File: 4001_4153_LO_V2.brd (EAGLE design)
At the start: 109 x 63 mm, 112 parts, among them IC1 74LVC2G17GV,125, IC10 MCP6H01, IC2 74LVC2G17GV,125, IC3 74LVC2G17GV,125, IC4 ADF4001BRUZ, IC5 ATTINY45V-10SU, IC6 7805DT, IC7 7809DT, IC8 LD117ASTR, IC9 ADF4153BRUZ-RL7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

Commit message: Tracking
Rotated 5v reg
tracking around output device
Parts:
- moved C41 0.38 mm to (94.5, 34.5)
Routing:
- net GND: track 64.2 -> 65.1 mm
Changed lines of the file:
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@@
 <layers>
 <layer number="1" name="Top" color="4" fill="1" visible="yes" active="yes"/>
-<layer number="2" name="RFEarth" color="1" fill="3" visible="no" active="yes"/>
+<layer number="2" name="RFEarth" color="1" fill="3" visible="yes" active="yes"/>
 <layer number="3" name="Route3" color="4" fill="3" visible="no" active="no"/>
 <layer number="4" name="Route4" color="1" fill="4" visible="no" active="no"/>
@@
 <layer number="13" name="Route13" color="4" fill="5" visible="no" active="no"/>
 <layer number="14" name="Route14" color="1" fill="6" visible="no" active="no"/>
-<layer number="15" name="Signal" color="4" fill="3" visible="no" active="yes"/>
+<layer number="15" name="Signal" color="4" fill="3" visible="yes" active="yes"/>
 <layer number="16" name="Power" color="1" fill="1" visible="yes" active="yes"/>
 <layer number="17" name="Pads" color="2" fill="1" visible="yes" active="yes"/>
@@
 <layer number="28" name="bValues" color="7" fill="1" visible="no" active="yes"/>
 <layer number="29" name="tStop" color="7" fill="3" visible="no" active="yes"/>
-<layer number="30" name="bStop" color="7" fill="6" visible="no" active="yes"/>
+<layer number="30" name="bStop" color="7" fill="6" visible="yes" active="yes"/>
 <layer number="31" name="tCream" color="7" fill="4" visible="no" active="yes"/>
 <layer number="32" name="bCream" color="7" fill="5" visible="no" active="yes"/>
@@
 <rectangle x1="88.854" y1="32.084" x2="123.854" y2="37.084" layer="30" rot="R90"/>
 <text x="4.863" y="3.556" size="1.016" layer="21" rot="R90">EXT REF</text>
-<text x="4.767" y="10.302" size="1.016" layer="21" rot="R90">EXT LOCK</text>
-<text x="4.798" y="18.2004" size="1.016" layer="21" rot="R90">VCO LOCK</text>
+<text x="4.767" y="18.302" size="1.016" layer="21" rot="R90">EXT LOCK</text>
+<text x="4.798" y="10.2004" size="1.016" layer="21" rot="R90">VCO LOCK</text>
 <wire x1="0" y1="53" x2="0" y2="1" width="0" layer="20"/>
 <wire x1="0" y1="1" x2="0" y2="-10" width="0" layer="20"/>
@@
 <rectangle x1="86" y1="50" x2="87" y2="53" layer="30"/>
 <rectangle x1="87" y1="49" x2="104" y2="53" layer="30"/>
+<rectangle x1="27" y1="0" x2="35" y2="9" layer="30"/>
 </plain>
 <attributes>
@@
 <attribute name="VALUE" x="98.0299" y="35.5929" size="1.27" layer="27" rot="R90"/>
 </element>
-<element name="C41" library="resistor" package="C0603" value="100pF" x="94.1672" y="34.492921875" smashed="yes">
-<attribute name="NAME" x="94.2942" y="32.460921875" size="1.27" layer="25"/>
-<attribute name="VALUE" x="93.2782" y="32.460921875" size="1.27" layer="27"/>
+<element name="C41" library="resistor" package="C0603" value="100pF" x="94.5482" y="34.492921875" smashed="yes">
+<attribute name="NAME" x="94.6752" y="32.460921875" size="1.27" layer="25"/>
+<attribute name="VALUE" x="93.6592" y="32.460921875" size="1.27" layer="27"/>
 </element>
 <element name="C31" library="resistor" package="C0603" value="1uF" x="91.521103125" y="41.4965625" smashed="yes" rot="R180">
@@
 <wire x1="43.559" y1="29.489" x2="42.480353125" y2="29.489" width="1.016" layer="1"/>
 <wire x1="42.480353125" y1="29.489" x2="42.288025" y2="29.296671875" width="1.016" layer="1"/>
-<wire x1="90.294071875" y1="34.4852375" x2="89.17449375" y2="34.4852375" width="1.27" layer="1"/>
 <wire x1="89.17449375" y1="34.4852375" x2="89.056546875" y2="34.603184375" width="1.27" layer="1"/>
 <contactref element="C15" pad="2"/>
@@
 <via x="25.803953125" y="8.870415625" extent="1-16" drill="0.8" shape="square"/>
 <via x="36.049753125" y="8.862015625" extent="1-16" drill="0.8" shape="square"/>
+<wire x1="90.294071875" y1="34.4852375" x2="89.2127625" y2="34.4852375" width="0.6096" layer="1"/>
+<wire x1="89.2127625" y1="34.4852375" x2="89.1286" y2="34.5694" width="0.6096" layer="1"/>
+<wire x1="89.1286" y1="34.5694" x2="89.1286" y2="34.8714" width="0.6096" layer="1"/>
+<wire x1="89.1286" y1="34.8714" x2="89" y2="35" width="0.6096" layer="1"/>
+<wire x1="89.17449375" y1="34.4852375" x2="89.17449375" y2="34.82550625" width="0.6096" layer="1"/>
+<wire x1="89.17449375" y1="34.82550625" x2="89.1286" y2="34.8714" width="0.6096" layer="1"/>
 </signal>
 <signal name="+9V">
@@
 <wire x1="93.9776" y1="32.6729375" x2="93.862121875" y2="32.557459375" width="0.6096" layer="1"/>
 <wire x1="91.994071875" y1="34.4852375" x2="93.309515625" y2="34.4852375" width="0.6096" layer="1"/>
-<wire x1="93.309515625" y1="34.4852375" x2="93.3172" y2="34.492921875" width="0.6096" layer="1"/>
+<wire x1="93.309515625" y1="34.4852375" x2="93.6982" y2="34.492921875" width="0.6096" layer="1"/>
 <wire x1="93.9776" y1="32.6729375" x2="93.9776" y2="33.1748" width="0.6096" layer="1"/>
 <wire x1="93.9776" y1="33.1748" x2="93.472" y2="33.6804" width="0.6096" layer="1"/>
 <wire x1="93.472" y1="33.6804" x2="93.472" y2="34.338121875" width="0.6096" layer="1"/>
-<wire x1="93.472" y1="34.338121875" x2="93.3172" y2="34.492921875" width="0.6096" layer="1"/>
+<wire x1="93.472" y1="34.338121875" x2="93.6982" y2="34.492921875" width="0.6096" layer="1"/>
 </signal>
 <signal name="+5V">
@@
 <contactref element="C41" pad="2"/>
 <contactref element="R17" pad="1"/>
-<wire x1="95.0172" y1="34.492921875" x2="97.303721875" y2="34.492921875" width="0.6096" layer="1"/>
+<wire x1="95.3982" y1="34.492921875" x2="97.303721875" y2="34.492921875" width="0.6096" layer="1"/>
 <wire x1="97.303721875" y1="34.492921875" x2="97.368" y2="34.5572" width="0.6096" layer="1"/>
 </signal>

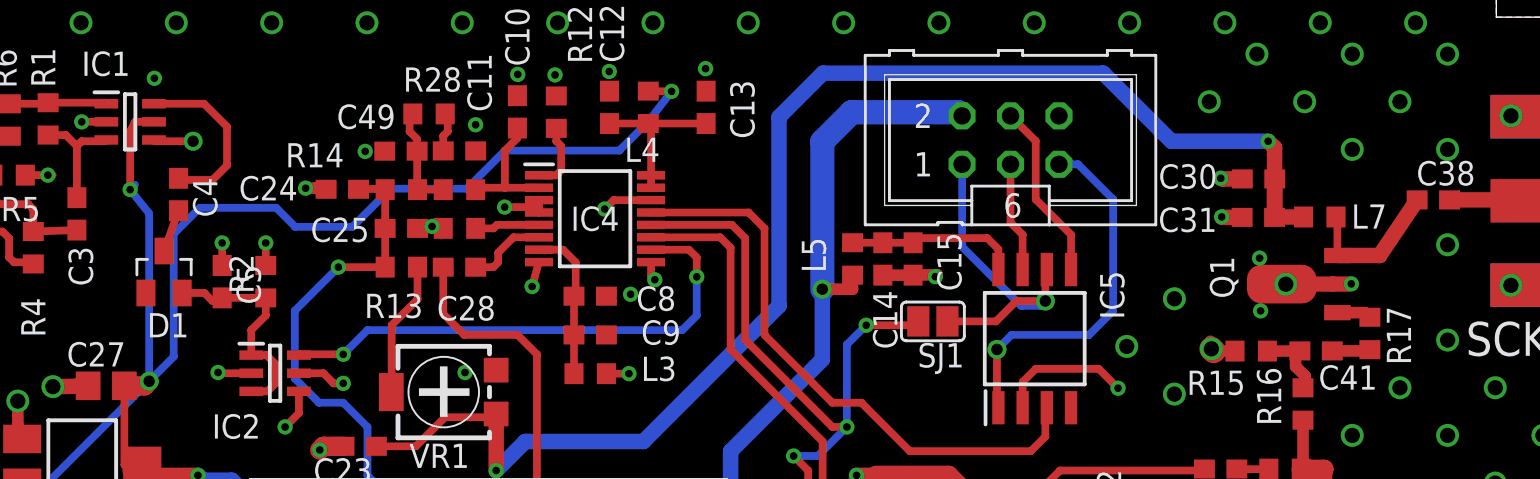
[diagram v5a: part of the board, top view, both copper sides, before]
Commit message: Output and detector
Moved resistor in output stage to power feed
Swapped C for R in 10MHz detector
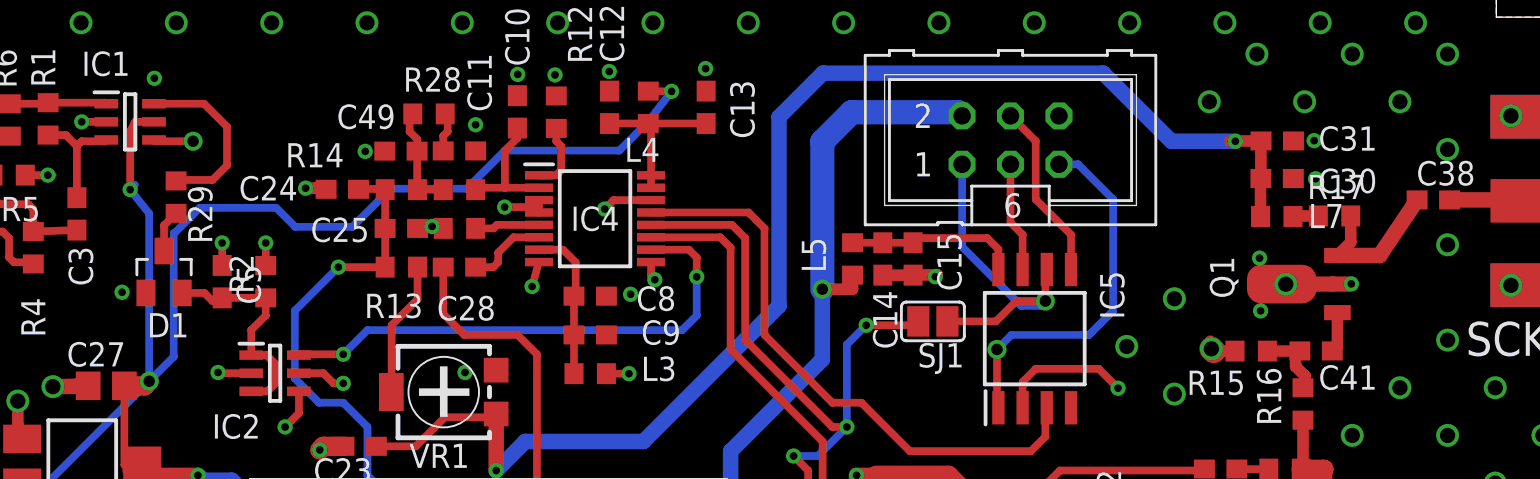
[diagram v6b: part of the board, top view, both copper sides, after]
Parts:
- removed C4: 100nF, resistor:C0603
- added R29: 100K, rcl:R0603
- IC8: value LD117ASTR -> LD1117AS33TR
- moved R17 6.44 mm to (95.5, 41.6), turned to 180 degrees
- moved C31 4.13 mm to (92.5, 45.5), turned to 0 degrees
- moved L7 2.26 mm to (92.5, 41.5)
- moved C30 0.97 mm to (92.5, 43.5), turned to 0 degrees
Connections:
- net N$11: now also C41.2; no longer R17.2
- net N$12: now also R17.1; no longer L7.1
- net N$21: now also L7.1, R17.2; no longer C41.2, R17.1
- net N$23: now also R29.2; no longer C4.2
- net N$30: now also R29.1; no longer C4.1
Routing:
- net +5V: track 136.2 -> 132.7 mm
- net GND: track 65.1 -> 62.9 mm
- net N$21: track 2.00 -> 1.34 mm

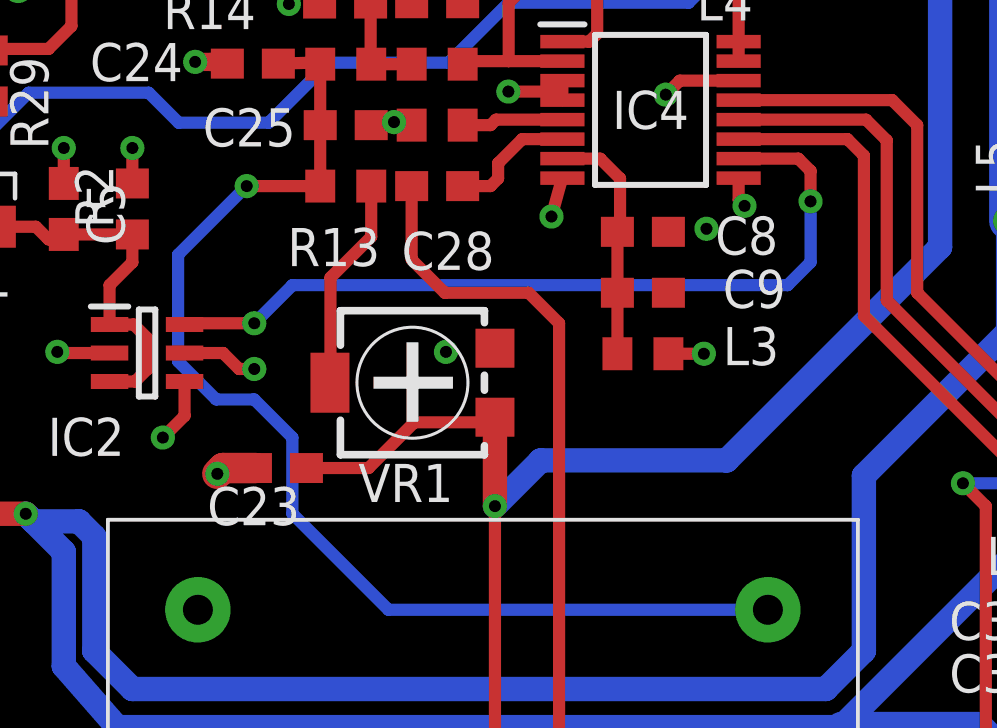
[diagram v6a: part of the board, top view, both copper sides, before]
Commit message: multi-turn
replaced single turn pot with multiturn
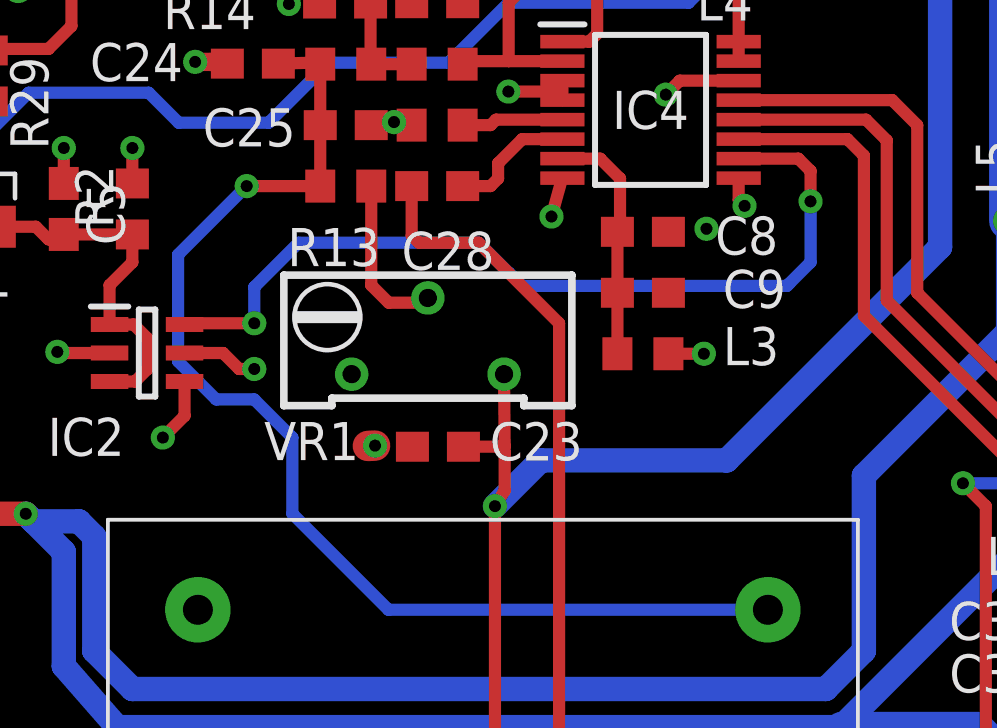
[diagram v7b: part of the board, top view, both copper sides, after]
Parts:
- VR1: value 1K -> (none); device resistor:RTRIM4G/J -> resistor:RTRIM64Y
- moved C23 5.28 mm to (49.6, 30.2)
- moved VR1 0.59 mm to (49.3, 32.6), turned to 270 degrees
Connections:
- net +5V: now also VR1.3; no longer VR1.1
- net GND: now also VR1.1; no longer VR1.3
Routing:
- net +5V: track 132.7 -> 128.7 mm
- net N$19: track 8.60 -> 5.50 mm
- net SDVDD1: track 27.3 -> 29.2 mm
- net GND: track 62.9 -> 61.8 mm, vias 188 -> 187
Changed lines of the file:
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@@
 <layers>
 <layer number="1" name="Top" color="4" fill="1" visible="yes" active="yes"/>
-<layer number="2" name="RFEarth" color="1" fill="3" visible="no" active="yes"/>
+<layer number="2" name="RFEarth" color="1" fill="3" visible="yes" active="yes"/>
 <layer number="3" name="Route3" color="4" fill="3" visible="no" active="no"/>
 <layer number="4" name="Route4" color="1" fill="4" visible="no" active="no"/>
@@
 <layer number="13" name="Route13" color="4" fill="5" visible="no" active="no"/>
 <layer number="14" name="Route14" color="1" fill="6" visible="no" active="no"/>
-<layer number="15" name="Signal" color="4" fill="3" visible="no" active="yes"/>
-<layer number="16" name="Power" color="1" fill="1" visible="yes" active="yes"/>
+<layer number="15" name="Signal" color="4" fill="3" visible="yes" active="yes"/>
+<layer number="16" name="Power" color="1" fill="1" visible="no" active="yes"/>
 <layer number="17" name="Pads" color="2" fill="1" visible="yes" active="yes"/>
 <layer number="18" name="Vias" color="2" fill="1" visible="yes" active="yes"/>
@@
 <attribute name="VALUE" x="18.172696875" y="22.532253125" size="1.27" layer="27"/>
 </element>
-<element name="VR1" library="resistor" package="RTRIM4G/J" value="1K" x="48.791759375" y="32.33279375" smashed="yes" rot="R90">
-<attribute name="NAME" x="46.988921875" y="28.3563375" size="1.27" layer="25"/>
-<attribute name="VALUE" x="51.331759375" y="36.37779375" size="1.27" layer="27" rot="R180"/>
-</element>
 <element name="IC8" library="v-reg" package="SOT223" value="LD1117AS33TR" x="29.83038125" y="27.5757625" smashed="yes" rot="R270">
 <attribute name="NAME" x="32.1142375" y="23.78518125" size="1.27" layer="25"/>
@@
 <attribute name="VALUE" x="79.496853125" y="13.551221875" size="1.27" layer="27" rot="R180"/>
 </element>
-<element name="C23" library="rcl" package="C0603" value="100nF" x="44.409" y="29.489" rot="R180"/>
+<element name="C23" library="rcl" package="C0603" value="100nF" x="49.6414" y="30.2002" smashed="yes" rot="R180">
+<attribute name="NAME" x="51.3744" y="29.7438" size="1.27" layer="25"/>
+<attribute name="VALUE" x="50.2764" y="32.1052" size="1.27" layer="27" rot="R180"/>
+</element>
 <element name="C14" library="resistor" package="C0603" value="1uF" x="71.823" y="39.3165" smashed="yes" rot="R270">
 <attribute name="NAME" x="71.315" y="37.6655" size="1.27" layer="25" rot="R270"/>
@@
 </element>
 <element name="R29" library="rcl" package="R0603" value="100K" x="34.752" y="42.559" rot="R270"/>
+<element name="VR1" library="resistor" package="RTRIM64Y" value="" x="49.3054" y="32.6186" smashed="yes" rot="R270">
+<attribute name="NAME" x="43.8474" y="29.753" size="1.27" layer="25"/>
+<attribute name="VALUE" x="44.3554" y="29.8686" size="1.27" layer="27"/>
+</element>
 </elements>
 <signals>
@@
 <contactref element="C20" pad="2"/>
 <contactref element="IC7" pad="3"/>
-<contactref element="VR1" pad="3"/>
 <via x="14.137003125" y="19.927146875" extent="1-16" drill="0.4" shape="square"/>
 <contactref element="C26" pad="2"/>
@@
 <via x="107.308184375" y="37.931953125" extent="1-16" drill="0.8" shape="square"/>
 <contactref element="C23" pad="2"/>
-<via x="42.288025" y="29.296671875" extent="1-16" drill="0.4" shape="square"/>
-<wire x1="43.559" y1="29.489" x2="42.480353125" y2="29.489" width="1.016" layer="1"/>
-<wire x1="42.480353125" y1="29.489" x2="42.288025" y2="29.296671875" width="1.016" layer="1"/>
+<via x="47.545825" y="30.236471875" extent="1-16" drill="0.4" shape="square"/>
+<wire x1="47.306353125" y1="30.2256" x2="47.545825" y2="30.236471875" width="1.016" layer="1"/>
 <wire x1="89.17449375" y1="34.4852375" x2="89.056546875" y2="34.603184375" width="1.27" layer="1"/>
 <contactref element="C15" pad="2"/>
@@
 <wire x1="38.696" y1="33.323" x2="36.991696875" y2="33.323" width="0.4064" layer="1"/>
 <wire x1="36.991696875" y1="33.323" x2="36.954025" y2="33.360671875" width="0.4064" layer="1"/>
-<via x="49.908025" y="33.360671875" extent="1-16" drill="0.4" shape="square"/>
 <wire x1="53.79" y1="41.752" x2="53.79" y2="42.402" width="0.4064" layer="1"/>
 <wire x1="53.607" y1="41.935" x2="53.79" y2="41.752" width="0.4064" layer="1"/>
@@
 <via x="94.520909375" y="43.5214625" extent="1-16" drill="0.4" shape="square"/>
 <via x="31.92" y="37.5712" extent="1-16" drill="0.4" shape="square"/>
+<contactref element="VR1" pad="1"/>
 </signal>
 <signal name="+9V">
@@
 <contactref element="C30" pad="1"/>
 <contactref element="C31" pad="1"/>
-<contactref element="VR1" pad="1"/>
 <contactref element="C23" pad="1"/>
 <contactref element="OSC1" pad="VCC"/>
@@
 <wire x1="48.6" y1="5.613" x2="41.792" y2="5.613" width="0.4064" layer="1"/>
 <wire x1="41.792" y1="5.613" x2="41.64" y2="5.765" width="0.4064" layer="1"/>
-<wire x1="45.259" y1="29.489" x2="47.33" y2="29.489" width="0.4064" layer="1"/>
-<wire x1="47.33" y1="29.489" x2="48.854" y2="31.013" width="0.4064" layer="1"/>
-<wire x1="48.854" y1="31.013" x2="51.371965625" y2="31.013" width="0.4064" layer="1"/>
-<wire x1="51.371965625" y1="31.013" x2="51.541759375" y2="31.18279375" width="0.4064" layer="1"/>
 <via x="90.3134" y="45.491" extent="1-16" drill="0.4" shape="octagon"/>
 <wire x1="90.3134" y1="45.491" x2="86.954" y2="45.491" width="0.8128" layer="16"/>
@@
 <wire x1="53.065759375" y1="29.743" x2="51.541759375" y2="28.219" width="0.8128" layer="16"/>
 <via x="51.541759375" y="28.219" extent="1-16" drill="0.4" shape="octagon"/>
-<wire x1="51.541759375" y1="28.219" x2="51.541759375" y2="31.18279375" width="0.8128" layer="1"/>
 <contactref element="IC6" pad="2"/>
 <contactref element="C17" pad="1"/>
@@
 <wire x1="91.661296875" y1="45.5050375" x2="90.0480375" y2="45.5050375" width="0.6096" layer="1"/>
 <wire x1="90.0480375" y1="45.5050375" x2="90.3134" y2="45.491" width="0.6096" layer="1"/>
+<contactref element="VR1" pad="3"/>
+<wire x1="51.8654" y1="30.2256" x2="51.8454" y2="32.6186" width="0.4064" layer="1"/>
+<wire x1="51.8654" y1="30.2256" x2="51.8654" y2="30" width="0.4064" layer="1"/>
+<wire x1="51.8654" y1="30" x2="51.8654" y2="28.733559375" width="0.4064" layer="1"/>
+<wire x1="51.8654" y1="28.733559375" x2="51.541759375" y2="28.219" width="0.4064" layer="1"/>
+<wire x1="50.4914" y1="30.2002" x2="51.6652" y2="30.2002" width="0.4064" layer="1"/>
+<wire x1="51.6652" y1="30.2002" x2="51.8654" y2="30" width="0.4064" layer="1"/>
 </signal>
 <signal name="OUTPUT">
@@
 <contactref element="C28" pad="2"/>
 <contactref element="OSC1" pad="OUT"/>
-<wire x1="48.766" y1="38.887" x2="48.766" y2="36.435" width="0.4064" layer="1"/>
-<wire x1="48.766" y1="36.435" x2="49.87" y2="35.331" width="0.4064" layer="1"/>
-<wire x1="49.87" y1="35.331" x2="52.664" y2="35.331" width="0.4064" layer="1"/>
-<wire x1="52.664" y1="35.331" x2="53.68" y2="34.315" width="0.4064" layer="1"/>
 <wire x1="53.68" y1="34.315" x2="53.68" y2="10.693" width="0.4064" layer="1"/>
 <wire x1="53.68" y1="10.693" x2="58.76" y2="5.613" width="0.4064" layer="1"/>
@@
 <wire x1="79.588" y1="9.677" x2="79.588" y2="11.389075" width="0.4064" layer="1"/>
 <wire x1="79.588" y1="11.389075" x2="79.457853125" y2="11.519221875" width="0.4064" layer="1"/>
+<wire x1="48.766" y1="38.887" x2="48.766" y2="37.234" width="0.4064" layer="1"/>
+<wire x1="48.766" y1="37.234" x2="49" y2="37" width="0.4064" layer="1"/>
+<wire x1="49" y1="37" x2="50.995" y2="37" width="0.4064" layer="1"/>
+<wire x1="50.995" y1="37" x2="53.68" y2="34.315" width="0.4064" layer="1"/>
 </signal>
 <signal name="LE_4153">
@@
 </signal>
 <signal name="N$19">
+<contactref element="R13" pad="1"/>
 <contactref element="VR1" pad="2"/>
-<contactref element="R13" pad="1"/>
-<wire x1="47.418" y1="38.887" x2="47.418" y2="37.197" width="0.4064" layer="1"/>
-<wire x1="47.418" y1="37.197" x2="46.06" y2="35.839" width="0.4064" layer="1"/>
-<wire x1="46.06" y1="35.839" x2="46.06" y2="31.589034375" width="0.4064" layer="1"/>
-<wire x1="46.06" y1="31.589034375" x2="46.041759375" y2="32.33279375" width="0.4064" layer="1"/>
+<wire x1="47.418" y1="38.887" x2="47.418" y2="35.582" width="0.4064" layer="1"/>
+<wire x1="47.418" y1="35.582" x2="48" y2="35" width="0.4064" layer="1"/>
+<wire x1="48" y1="35" x2="49.1468" y2="35" width="0.4064" layer="1"/>
+<wire x1="49.1468" y1="35" x2="49.3054" y2="35.1586" width="0.4064" layer="1"/>
 </signal>
 <signal name="4001_CP">
@@
 <via x="62.062" y="38.379" extent="1-16" drill="0.4" shape="octagon"/>
 <wire x1="62.062" y1="38.379" x2="62.062" y2="36.347" width="0.4064" layer="16"/>
-<wire x1="62.062" y1="36.347" x2="61.3" y2="35.585" width="0.4064" layer="16"/>
-<wire x1="61.3" y1="35.585" x2="44.79" y2="35.585" width="0.4064" layer="16"/>
-<wire x1="44.79" y1="35.585" x2="43.52" y2="34.315" width="0.4064" layer="16"/>
+<wire x1="62.062" y1="36.347" x2="61.3575" y2="35.6425" width="0.4064" layer="16"/>
+<wire x1="61.3575" y1="35.6425" x2="61.3" y2="35.585" width="0.4064" layer="16"/>
 <via x="43.52" y="34.315" extent="1-16" drill="0.4" shape="octagon"/>
 <wire x1="43.52" y1="34.315" x2="41.238" y2="34.315" width="0.4064" layer="1"/>
 <wire x1="41.238" y1="34.315" x2="41.196" y2="34.273" width="0.4064" layer="1"/>
+<wire x1="43.52" y1="34.315" x2="43.52" y2="35.52" width="0.4064" layer="16"/>
+<wire x1="43.52" y1="35.52" x2="45" y2="37" width="0.4064" layer="16"/>
+<wire x1="45" y1="37" x2="51" y2="37" width="0.4064" layer="16"/>
+<wire x1="51" y1="37" x2="52" y2="36" width="0.4064" layer="16"/>
+<wire x1="52" y1="36" x2="52.011" y2="36" width="0.4064" layer="16"/>
+<wire x1="52.011" y1="36" x2="52.451" y2="35.56" width="0.4064" layer="16"/>
+<wire x1="52.451" y1="35.56" x2="61.275" y2="35.56" width="0.4064" layer="16"/>
+<wire x1="61.275" y1="35.56" x2="61.3" y2="35.585" width="0.4064" layer="16"/>
 </signal>
 <signal name="DVDD1">
